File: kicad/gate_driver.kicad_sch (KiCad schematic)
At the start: 37 parts, among them U1 DRV8301DCAR, U4 SN74LVC1G66DCKR, U5 SN74LVC1G66DCKR, U6 SN74LVC1G66DCKR

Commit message: checking shunt footprints
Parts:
- removed C3: 120pF, Capacitor_SMD:C_0402_1005Metric, symbol Device:C
- removed C8: 2.2uF, Capacitor_SMD:C_0402_1005Metric, symbol Device:C
- removed R2: 220k, Resistor_SMD:R_0402_1005Metric, symbol Device:R
- added C31: 120pF, Capacitor_SMD:C_0402_1005Metric, symbol Device:C
- added R21: 220k, Resistor_SMD:R_0402_1005Metric, symbol Device:R
- C20: renamed from C26; footprint (none) -> Capacitor_SMD:CP_Elec_5x5.4
- C24: renamed from C6; value 2.2uF -> 1uF
- renumbered C27 to C18, C9 to C19, C25 to C21, C30 to C22, C5 to C23, C10 to C25, C28 to C26, C11 to C27, C23 to C28, C24 to C29, C31 to C30, C4 to C32, C29 to C33, C7 to C34, C32 to C35, D1 to D8, R10 to R19, R9 to R20, R4 to R22, R11 to R23, R5 to R24, R8 to R25, R12 to R26, R3 to R27, R15 to R28, R13 to R29, R14 to R30, U4 to U3, U1 to U4
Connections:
- net COMP: now also C31.1
- net GND: now also C31.2, R21.1
- net at U4.1 (RT_CLK): now also R21.2

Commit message: gate driver routed to mosfets, working on misc stm32 related components
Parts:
- L1: footprint Inductor_SMD:L_0402_1005Metric -> footprints:IND_VLS3010CX-220M-1
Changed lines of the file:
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@@
 			)
 		)
-		(property "Footprint" "Inductor_SMD:L_0402_1005Metric"
+		(property "Footprint" "footprints:IND_VLS3010CX-220M-1"
 			(at 95.25 44.45 0)
 			(effects

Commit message: done? without test points
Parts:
- U3, U5, U6: footprint footprints:SOT65P210X110-5N -> footprints:SOT65P210X110-5N_Custom
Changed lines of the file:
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@@
 			)
 		)
-		(property "Footprint" "footprints:SOT65P210X110-5N"
+		(property "Footprint" "footprints:SOT65P210X110-5N_Custom"
 			(at 45.974 57.912 0)
 			(effects
@@
 			)
 		)
-		(property "Footprint" "footprints:SOT65P210X110-5N"
+		(property "Footprint" "footprints:SOT65P210X110-5N_Custom"
 			(at 45.974 115.062 0)
 			(effects
@@
 			)
 		)
-		(property "Footprint" "footprints:SOT65P210X110-5N"
+		(property "Footprint" "footprints:SOT65P210X110-5N_Custom"
 			(at 45.974 173.482 0)
 			(effects

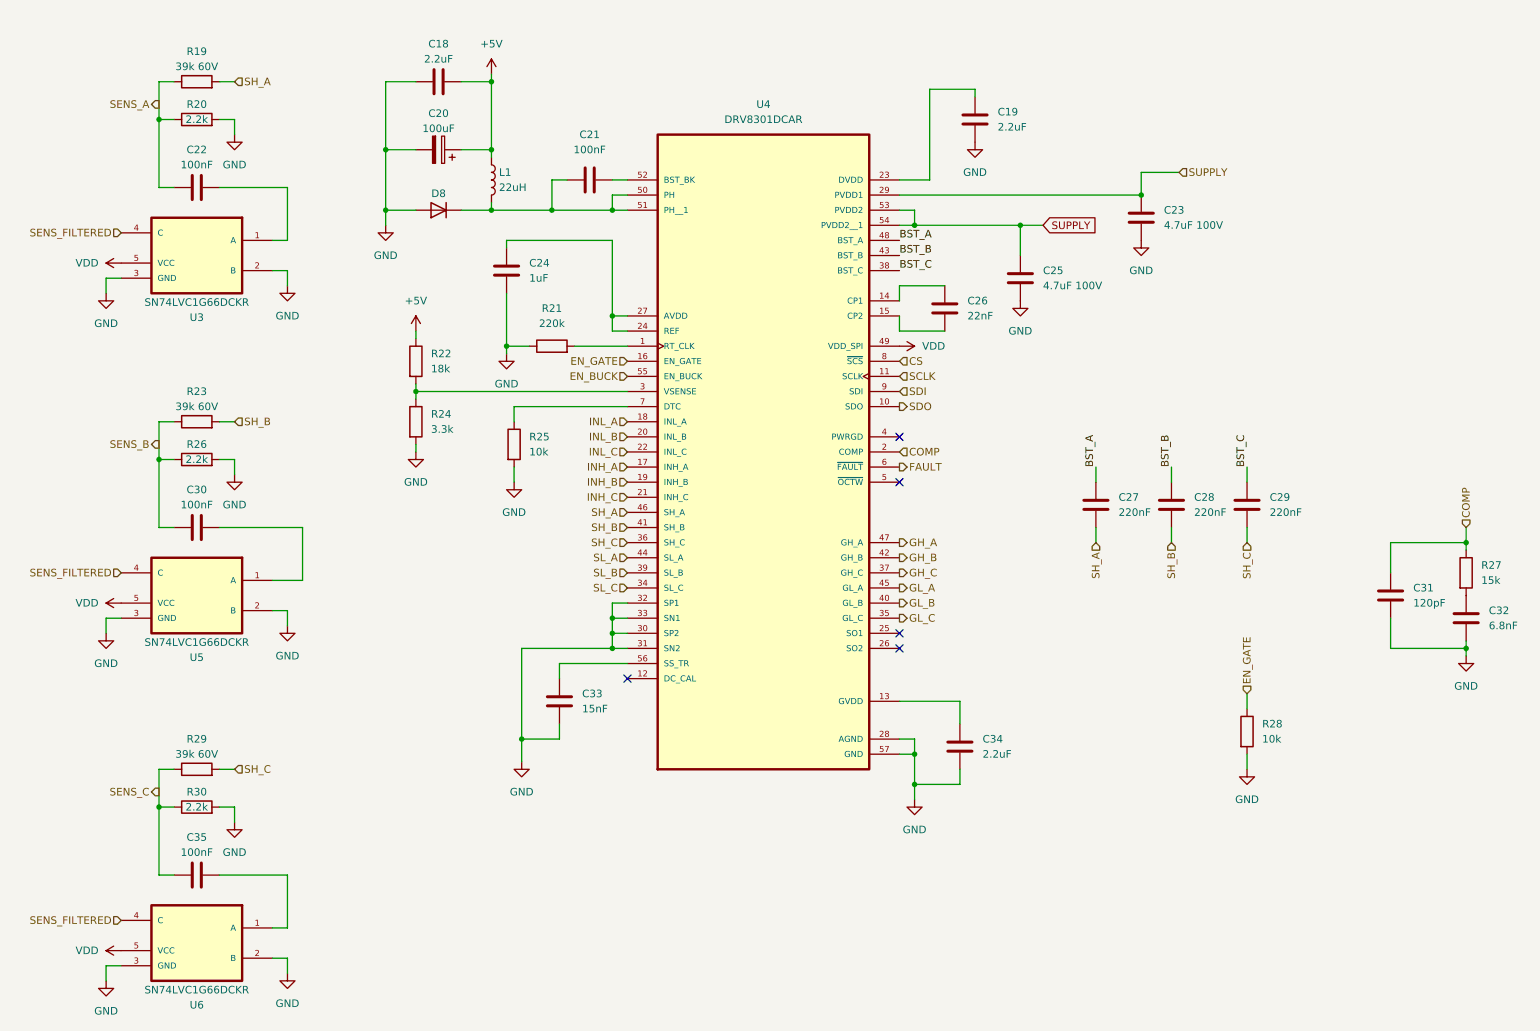
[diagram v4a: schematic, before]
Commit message: finalizing schematic for gate driver
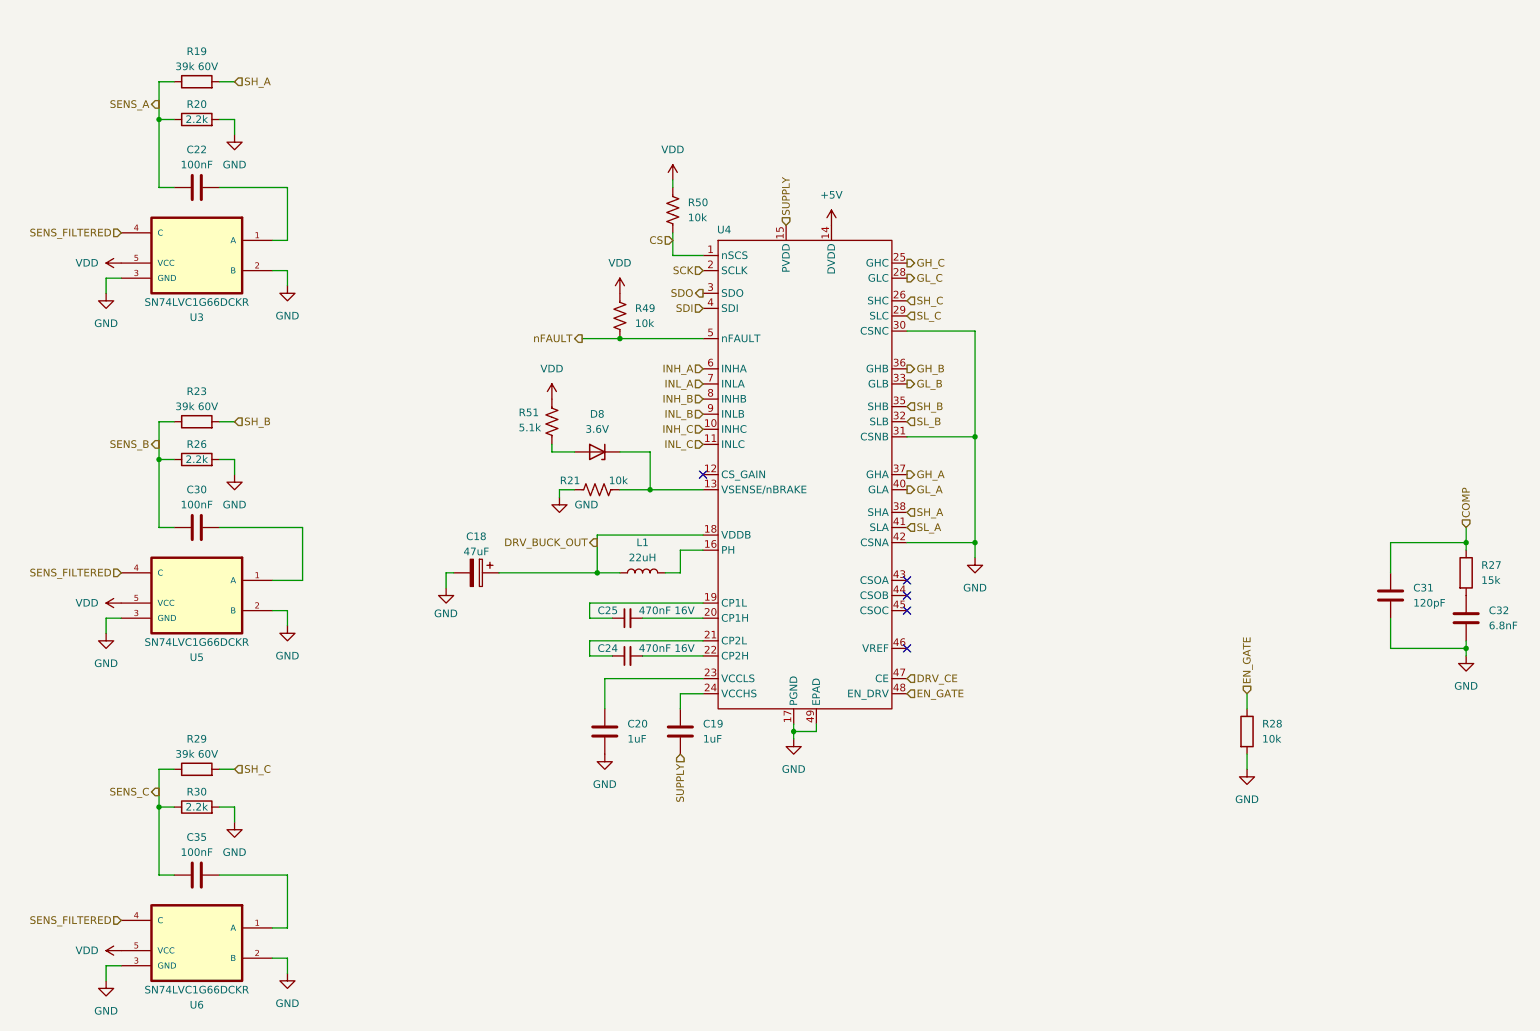
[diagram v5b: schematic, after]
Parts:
- removed C18, C34: 2.2uF, Capacitor_SMD:C_0402_1005Metric, symbol Device:C
- removed C20: 100uF, Capacitor_SMD:CP_Elec_5x5.4, symbol Device:C_Polarized
- removed C21: 100nF, Capacitor_SMD:C_0402_1005Metric, symbol Device:C
- removed C23, C25: 4.7uF 100V, Capacitor_SMD:C_1210_3225Metric, symbol Device:C
- removed C24: 1uF, Capacitor_SMD:C_0402_1005Metric, symbol Device:C
- removed C26: 22nF, Capacitor_SMD:C_0402_1005Metric, symbol Device:C
- removed C27, C28, C29: 220nF, Capacitor_SMD:C_0402_1005Metric, symbol Device:C
- removed C33: 15nF, Capacitor_SMD:C_0402_1005Metric, symbol Device:C
- removed D8: ~, Diode_SMD:D_SOD-323, symbol Device:D
- removed R21: 220k, Resistor_SMD:R_0402_1005Metric, symbol Device:R
- removed R22: 18k, Resistor_SMD:R_0402_1005Metric, symbol Device:R
- removed R24: 3.3k, Resistor_SMD:R_0402_1005Metric, symbol Device:R
- removed R25: 10k, Resistor_SMD:R_0402_1005Metric, symbol Device:R
- removed U4: DRV8301DCAR, footprints:SOP50P810X120-57N, symbol DRV8301DCAR:DRV8301DCAR
- added C18: 47uF, Capacitor_SMD:CP_Elec_5x5.3, symbol Device:C_Polarized
- added C20: 1uF, Capacitor_SMD:C_0402_1005Metric, symbol Device:C
- added C24, C25: 470nF 16V, Capacitor_SMD:C_0402_1005Metric, symbol Device:C_Small
- added D8: 3.6V, Diode_SMD:D_SOD-323_HandSoldering, symbol Device:D_Zener
- added R21, R49, R50: 10k, Resistor_SMD:R_0402_1005Metric, symbol Device:R_US
- added R51: 5.1k, Resistor_SMD:R_0402_1005Metric, symbol Device:R_US
- added U4: ~, footprints:QFN48P700X700X90, symbol custom:6EDL7141
- C19: value 2.2uF -> 1uF
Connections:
- net +5V: now also U4.14 (DVDD); no longer L1.1
- net CS: now also R50.1, U4.1 (nSCS)
- net EN_GATE: now also U4.48 (EN_DRV)
- net GH_A: now also U4.37 (GHA)
- net GH_B: now also U4.36 (GHB)
- net GH_C: now also U4.25 (GHC)
- net GL_A: now also U4.40 (GLA)
- net GL_B: now also U4.33 (GLB)
- net GL_C: now also U4.28 (GLC)
- net GND: now also C18.2, C20.2, R21.1, U4.17 (PGND), U4.30 (CSNC), U4.31 (CSNB), U4.42 (CSNA), U4.49 (EPAD); no longer C19.2
- net INH_A: now also U4.6 (INHA)
- net INH_B: now also U4.8 (INHB)
- net INH_C: now also U4.10 (INHC)
- net INL_A: now also U4.7 (INLA)
- net INL_B: now also U4.9 (INLB)
- net INL_C: now also U4.11 (INLC)
- net SDI: now also U4.4 (SDI)
- net SDO: now also U4.3 (SDO)
- net SH_A: now also U4.38 (SHA)
- net SH_B: now also U4.35 (SHB)
- net SH_C: now also U4.26 (SHC)
- net SL_A: now also U4.41 (SLA)
- net SL_B: now also U4.32 (SLB)
- net SL_C: now also U4.29 (SLC)
- net SUPPLY: now also C19.2, U4.15 (PVDD)
- net VDD: now also R49.1, R50.2, R51.1
- net at L1.2: now also U4.16 (PH)
- net at C19.1: now also U4.24 (VCCHS)
- new net: C25.1, U4.19 (CP1L)
- new net: C25.2, U4.20 (CP1H)
- new net: D8.1 (K), R21.2, U4.13 (VSENSE/nBRAKE)
- new net: C20.1, U4.23 (VCCLS)
- new net: D8.2 (A), R51.2
- new net: C24.1, U4.21 (CP2L)
- new net: C24.2, U4.22 (CP2H)
- new net DRV_BUCK_OUT: C18.1, L1.1, U4.18 (VDDB)
- new net DRV_CE: U4.47 (CE)
- new net SCK: U4.2 (SCLK)
- new net nFAULT: R49.2, U4.5 (nFAULT)
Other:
- moved on the sheet: L1

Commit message: revert to v6.05
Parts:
- removed C31: 120pF, Capacitor_SMD:C_0402_1005Metric, symbol Device:C
- removed C32: 6.8nF, Capacitor_SMD:C_0402_1005Metric, symbol Device:C
- removed R27: 15k, Resistor_SMD:R_0402_1005Metric, symbol Device:R
- removed R28: 10k, Resistor_SMD:R_0402_1005Metric, symbol Device:R
- added C21: 100nF 63V, Capacitor_SMD:C_0603_1608Metric, symbol Device:C
- added R25: 0R, Resistor_SMD:R_0402_1005Metric, symbol Device:R_US
- added TP12: nBRAKE, TestPoint:TestPoint_Pad_D1.0mm, symbol Connector:TestPoint
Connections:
- net +5V: now also R25.1; no longer U4.14 (DVDD)
- net GND: now also C21.2
- net SUPPLY: now also C21.1
- net at D8.1 (K), R21.2, U4.13 (VSENSE/nBRAKE): now also TP12.1
- new net: R25.2, U4.14 (DVDD)

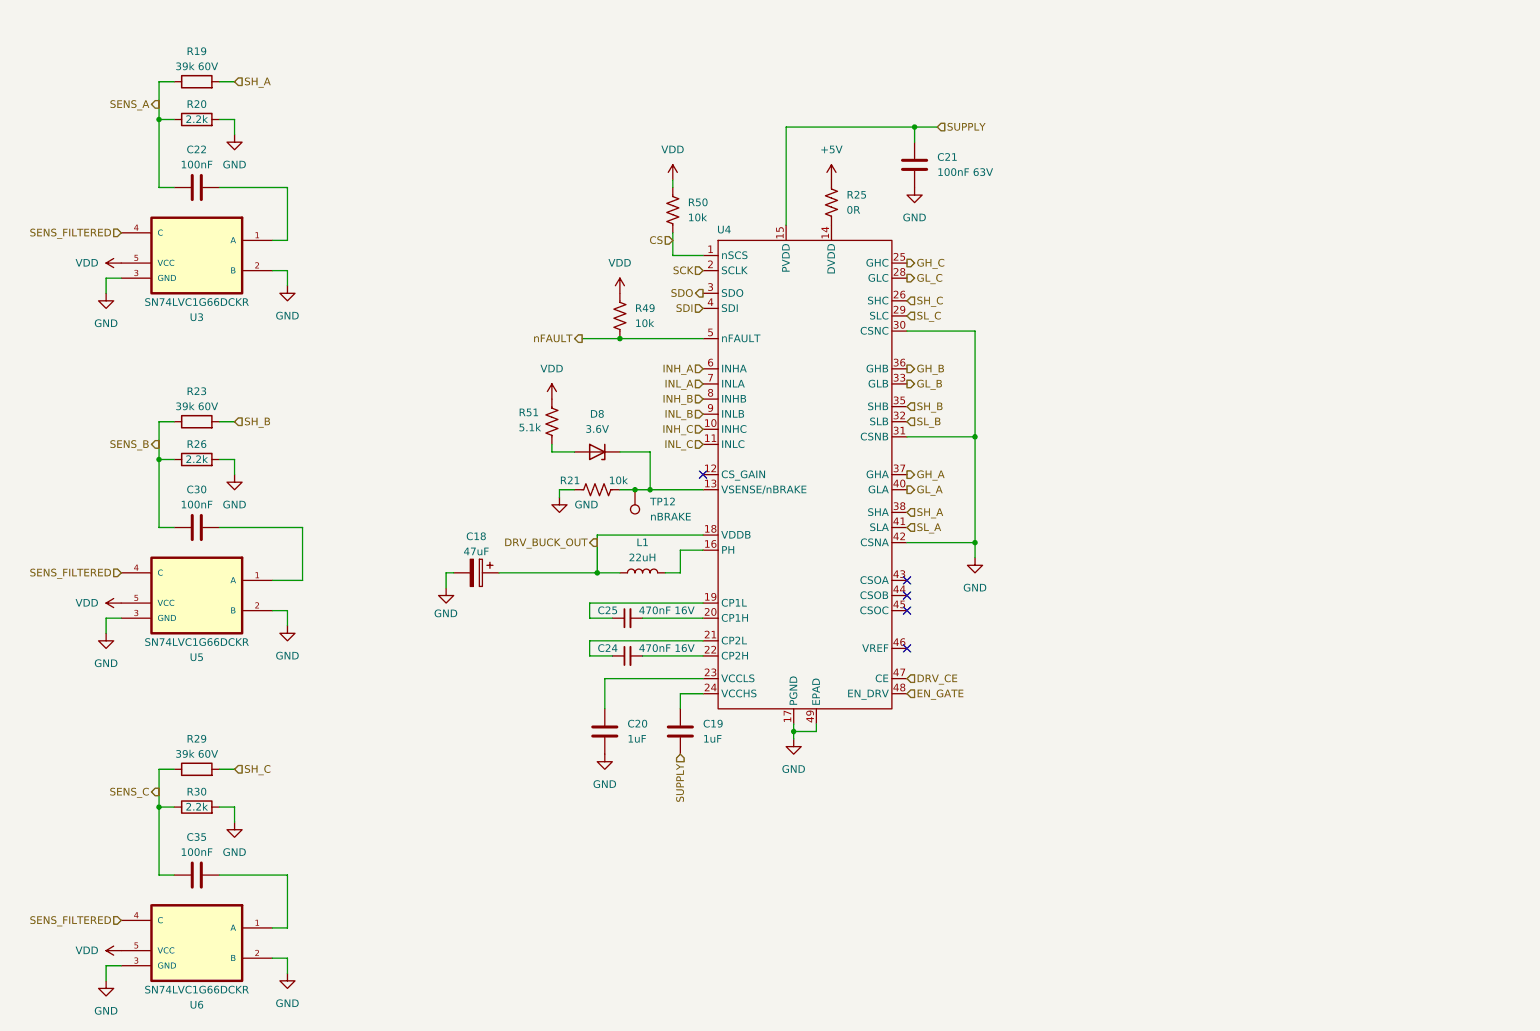
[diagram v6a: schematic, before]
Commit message: gate driver mostly schematic'd and pcb started
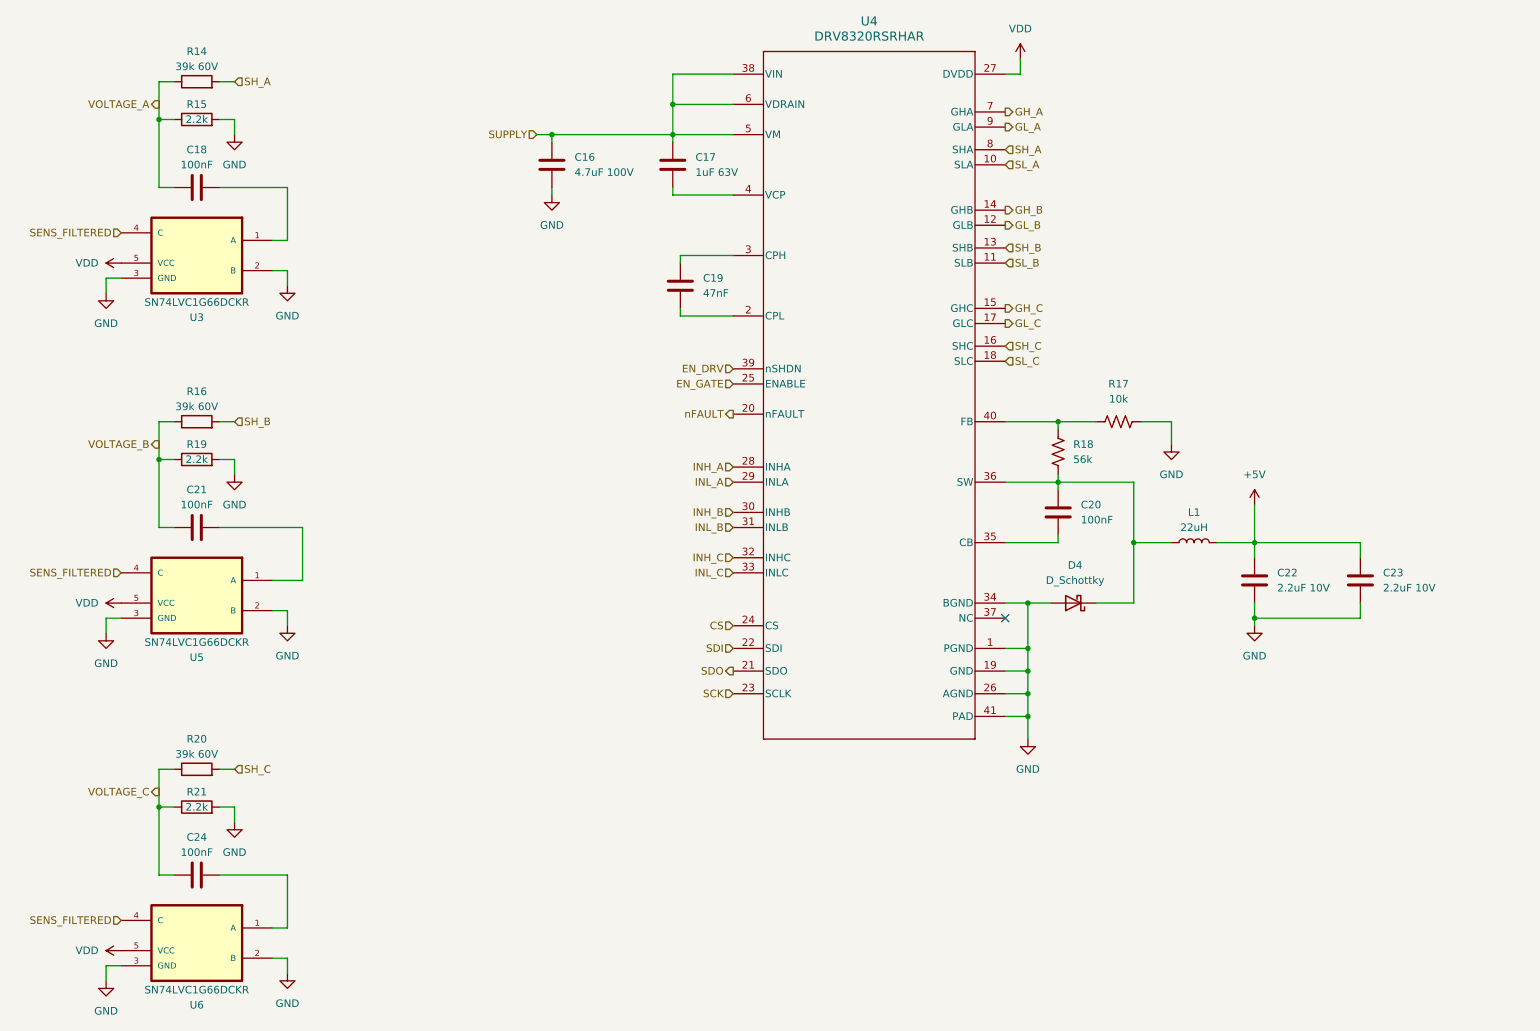
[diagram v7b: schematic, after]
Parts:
- removed C18: 47uF, Capacitor_SMD:CP_Elec_5x5.3, symbol Device:C_Polarized
- removed C24, C25: 470nF 16V, Capacitor_SMD:C_0402_1005Metric, symbol Device:C_Small
- removed D8: 3.6V, Diode_SMD:D_SOD-323_HandSoldering, symbol Device:D_Zener
- removed R21, R49, R50: 10k, Resistor_SMD:R_0402_1005Metric, symbol Device:R_US
- removed R25: 0R, Resistor_SMD:R_0402_1005Metric, symbol Device:R_US
- removed R51: 5.1k, Resistor_SMD:R_0402_1005Metric, symbol Device:R_US
- removed TP12: nBRAKE, TestPoint:TestPoint_Pad_D1.0mm, symbol Connector:TestPoint
- removed U4: ~, footprints:QFN48P700X700X90, symbol custom:6EDL7141
- added C17: 1uF 63V, Capacitor_SMD:C_0805_2012Metric, symbol Device:C
- added C22, C23: 2.2uF 10V, Capacitor_SMD:C_0603_1608Metric, symbol Device:C
- added D4: D_Schottky, symbol Device:D_Schottky
- added R17: 10k, Resistor_SMD:R_0402_1005Metric, symbol Device:R_US
- added R18: 56k, Resistor_SMD:R_0402_1005Metric, symbol Device:R_US
- added U4: DRV8320RSRHAR, footprints:RHA0040B_NV, symbol DRV8320RS:DRV8320RSRHAR
- C16: renamed from C21; value 100nF 63V -> 4.7uF 100V; footprint Capacitor_SMD:C_0603_1608Metric -> Capacitor_SMD:C_1206_3216Metric
- C19: value 1uF -> 47nF
- C20: value 1uF -> 100nF
- L1: footprint footprints:IND_VLS3010CX-220M-1 -> (none)
- renumbered C22 to C18, C30 to C21, C35 to C24, R19 to R14, R20 to R15, R23 to R16, R26 to R19, R29 to R20, R30 to R21
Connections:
- net DRV_BUCK_OUT is gone; now on an unnamed net: L1.1
- net +5V: now also L1.2, C22.1, C23.1
- net CS: now also U4.24 (CS)
- net EN_GATE: now also U4.25 (ENABLE)
- net GH_A: now also U4.7 (GHA)
- net GH_B: now also U4.14 (GHB)
- net GH_C: now also U4.15 (GHC)
- net GL_A: now also U4.9 (GLA)
- net GL_B: now also U4.12 (GLB)
- net GL_C: now also U4.17 (GLC)
- net GND: now also C22.2, C23.2, D4.2 (A), R17.2, U4.1 (PGND), U4.19 (GND), U4.26 (AGND), U4.34 (BGND), U4.41 (PAD); no longer C20.2
- net INH_A: now also U4.28 (INHA)
- net INH_B: now also U4.30 (INHB)
- net INH_C: now also U4.32 (INHC)
- net INL_A: now also U4.29 (INLA)
- net INL_B: now also U4.31 (INLB)
- net INL_C: now also U4.33 (INLC)
- net SCK: now also U4.23 (SCLK)
- net SDI: now also U4.22 (SDI)
- net SDO: now also U4.21 (SDO)
- net SH_A: now also U4.8 (SHA)
- net SH_B: now also U4.13 (SHB)
- net SH_C: now also U4.16 (SHC)
- net SL_A: now also U4.10 (SLA)
- net SL_B: now also U4.11 (SLB)
- net SL_C: now also U4.18 (SLC)
- net SUPPLY: now also C17.1, U4.38 (VIN), U4.5 (VM), U4.6 (VDRAIN); no longer C19.2
- net VDD: now also U4.27 (DVDD)
- net nFAULT: now also U4.20 (nFAULT)
- net at C20.1: now also D4.1 (K), R18.2, U4.36 (SW)
- net at C19.1: now also U4.3 (CPH)
- net SENS_A renamed VOLTAGE_A
- net SENS_B renamed VOLTAGE_B
- net SENS_C renamed VOLTAGE_C
- new net: C19.2, U4.2 (CPL)
- new net: C20.2, U4.35 (CB)
- new net: C17.2, U4.4 (VCP)
- new net: R17.1, R18.1, U4.40 (FB)
- new net EN_DRV: U4.39 (nSHDN)
- no-connect marks 5 -> 1
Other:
- moved on the sheet: C16

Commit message: rev3 ordered
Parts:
- added NT4: NetTie_2, footprints:NetTie-2_SMD_Pad0.2mm, symbol Device:NetTie_2
- C21: renamed from C16; footprint Capacitor_SMD:C_1206_3216Metric -> Capacitor_SMD:C_1210_3225Metric
- C23: renamed from C22; footprint Capacitor_SMD:C_0603_1608Metric -> Capacitor_SMD:C_0402_1005Metric
- C24: renamed from C23; footprint Capacitor_SMD:C_0603_1608Metric -> Capacitor_SMD:C_0402_1005Metric
- D8: renamed from D4; footprint (none) -> Diode_SMD:D_SOD-323_HandSoldering
- L1: footprint (none) -> footprints:IND_VLS3010CX-220M-1
- R19: renamed from R14; symbol Device:R -> Device:R_US
- R20: renamed from R15; symbol Device:R -> Device:R_US
- R23: renamed from R16; symbol Device:R -> Device:R_US
- R26: renamed from R19; symbol Device:R -> Device:R_US
- R29: renamed from R20; symbol Device:R -> Device:R_US
- R30: renamed from R21; symbol Device:R -> Device:R_US
- renumbered C19 to C18, C17 to C19, C18 to C22, C21 to C30, C24 to C35, R18 to R21, R17 to R22
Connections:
- net EN_GATE is gone; now on net EN_DRV: U4.25 (ENABLE)
- net +5V: now also R21.2
- net EN_DRV: no longer U4.39 (nSHDN)
- net GND: now also R22.1; no longer R22.2
- net SUPPLY: now also NT4.1; no longer U4.6 (VDRAIN)
- net at C20.1, D8.1 (K), L1.1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: no longer R21.2
- net at R21.1, U4.40 (FB): now also R22.2; no longer R22.1
- new net: NT4.2, U4.6 (VDRAIN)
- new net nSHDN: U4.39 (nSHDN)
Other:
- moved on the sheet: C18, L1, R21, R22
